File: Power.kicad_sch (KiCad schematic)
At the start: 19 parts, among them U601 HT7463A, U602 BD2243G, U603 MIC5504-3.3YM5

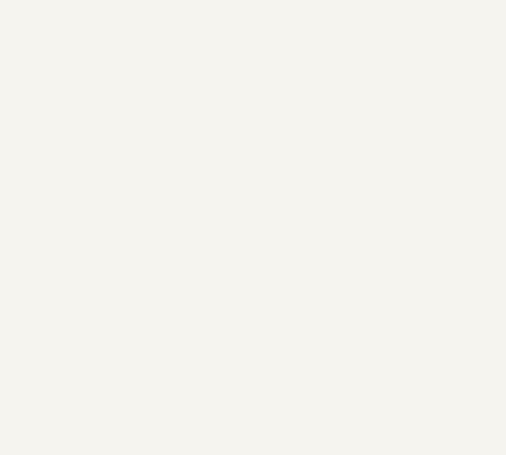
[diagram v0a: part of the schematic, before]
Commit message: Added 'Power', 'Op' and 'Error' LEDs
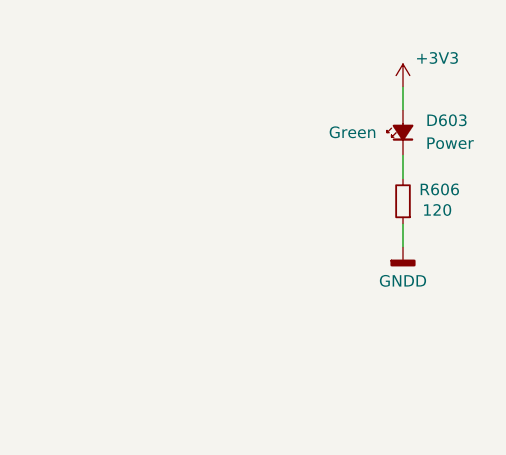
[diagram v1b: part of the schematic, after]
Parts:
- added D603: Power, LED_SMD:LED_0603_1608Metric, symbol Device:LED_Small_Filled
- added R606: 120, Resistor_SMD:R_0603_1608Metric, symbol Device:R_Small
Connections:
- net +3V3: now also D603.2 (A)
- net GNDD: now also R606.1
- new net: D603.1 (K), R606.2

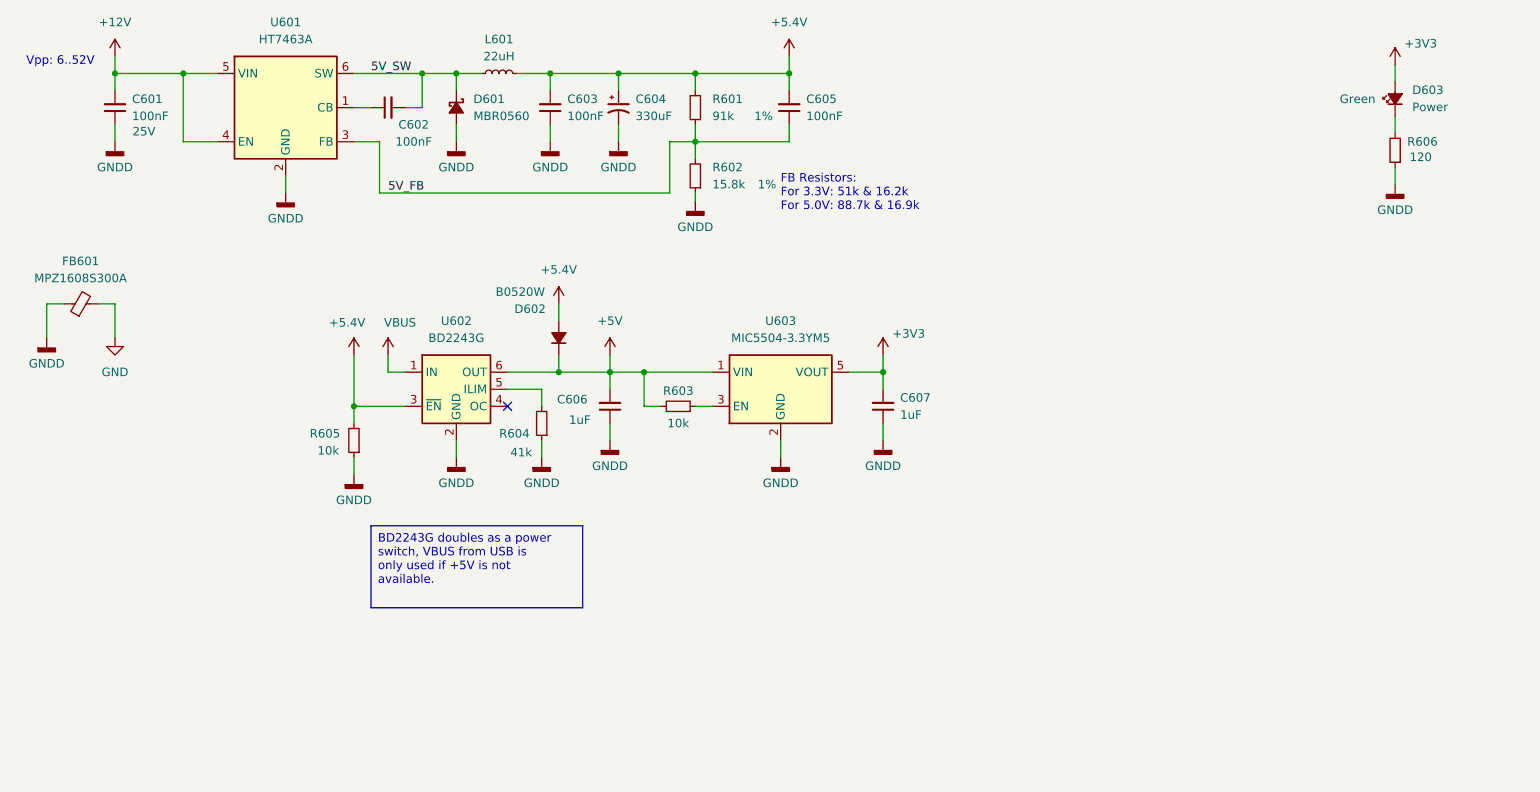
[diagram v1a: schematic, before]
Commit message: Created PDF of schematic
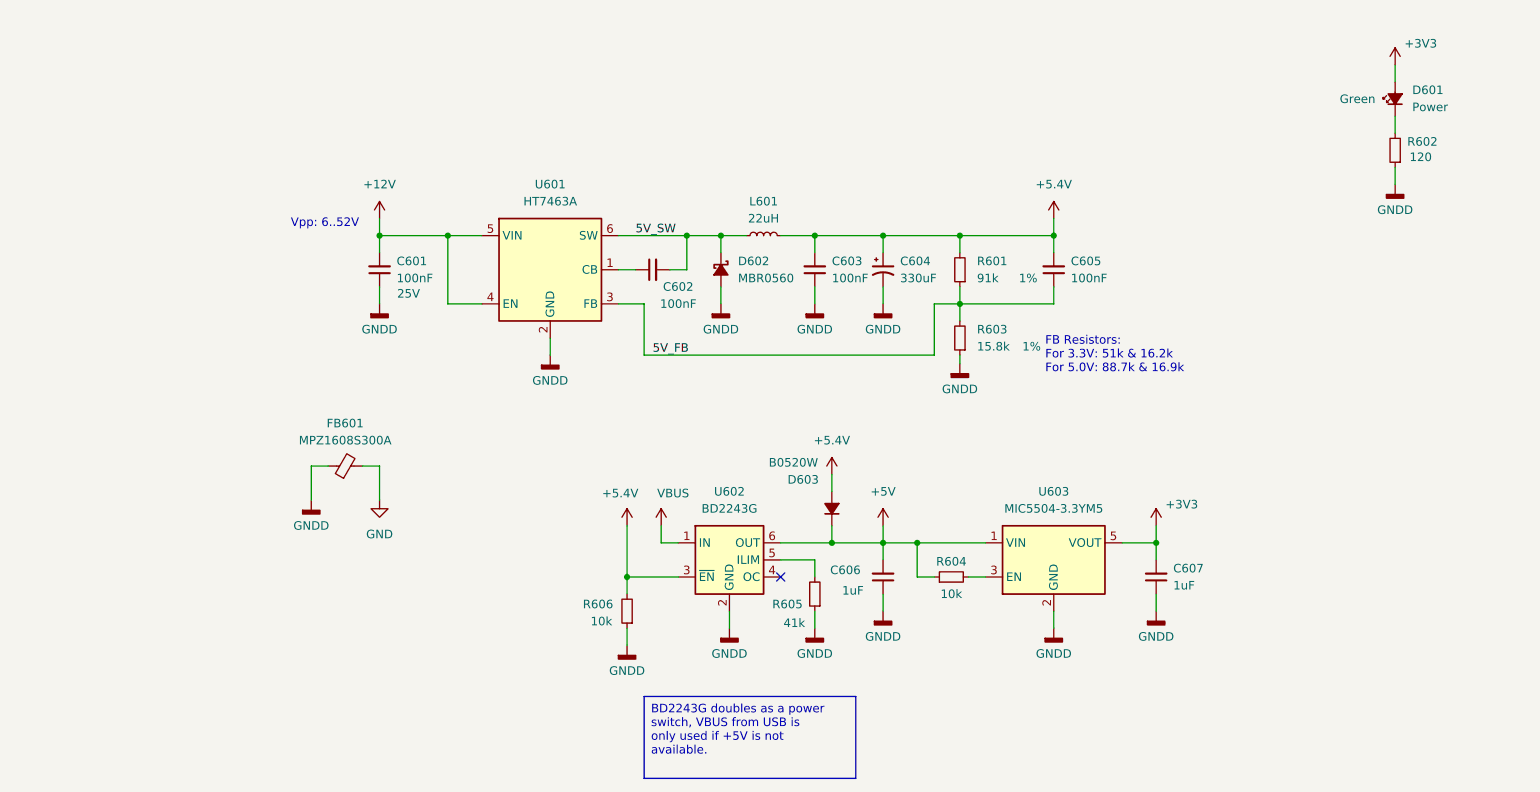
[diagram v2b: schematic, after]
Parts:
- renumbered D603 to D601, D601 to D602, D602 to D603, R606 to R602, R602 to R603, R603 to R604, R604 to R605, R605 to R606
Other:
- company: (none) -> TiZed
- title: (none) -> Power
- moved on the sheet: C601, C602, C603, C604, C605, C606, C607, D602, D603, FB601, L601, R601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

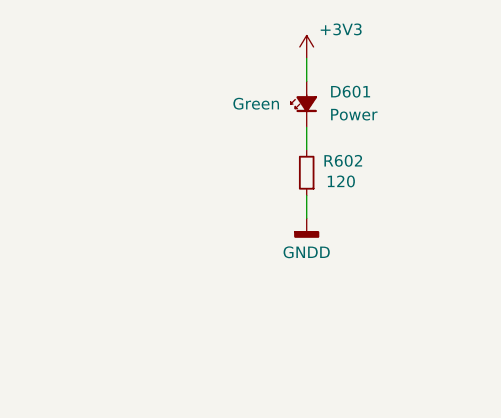
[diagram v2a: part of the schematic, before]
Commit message: Added LEDs part numbers
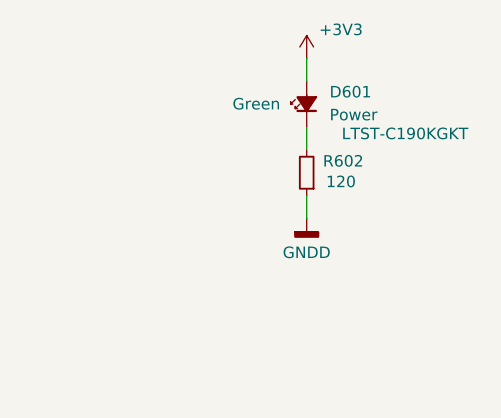
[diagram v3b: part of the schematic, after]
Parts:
- D601: Part (none) -> LTST-C190KGKT
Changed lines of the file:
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@@
+			)
+		)
+		(property "Part" "LTST-C190KGKT "
+			(at 239.522 38.862 90)
+			(effects
+				(font
+					(size 1.27 1.27)
+				)
 			)
 		)

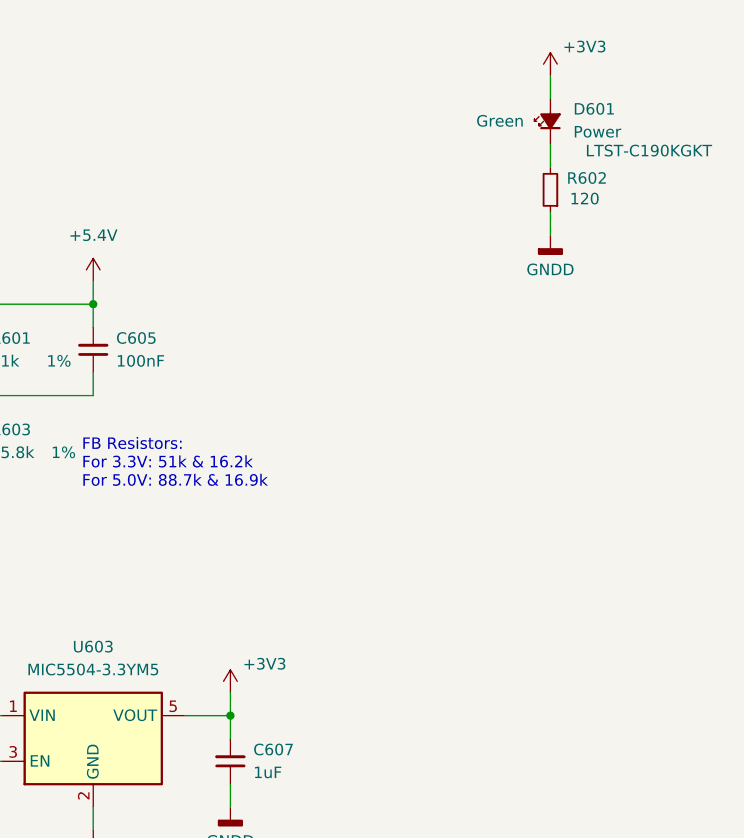
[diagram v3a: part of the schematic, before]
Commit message: Schematic fixes for PCB layout
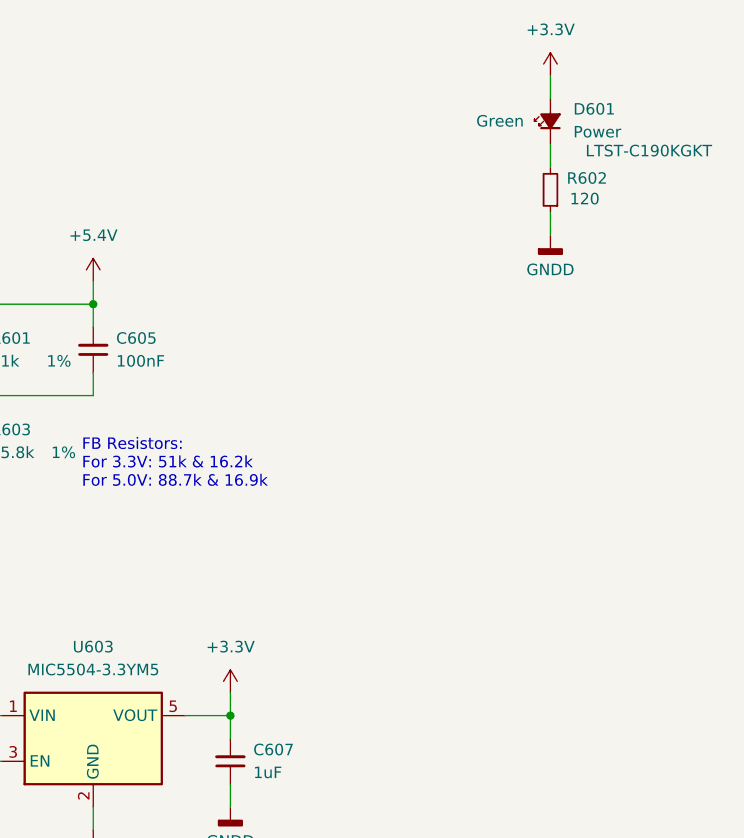
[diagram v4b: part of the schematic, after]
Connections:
- net +3V3 renamed +3.3V
